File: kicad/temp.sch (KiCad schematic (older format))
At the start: 44 parts, among them U901 ADM2483, U902 AMC1311B, U903 AMC1311B, U904 AMC1311B, U905 AMC1311B

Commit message: changing single row terminal block to double row
I've changed to double row all the connectors, RJ45 and terminal blocks,
I saves spaces and also make it more intuitive related to user
interface..lets go
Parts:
- renumbered C909 to C902, C910 to C904, C907 to C905, C911 to C906, C905 to C907, C912 to C908, C902 to C909, C913 to C910, C904 to C911, C914 to C912, C906 to C913, C915 to C914, C908 to C915, R914 to R903, R915 to R904, R908 to R905, R916 to R906, R905 to R907, R906 to R908, R907 to R909, R917 to R912, R918 to R913, R903 to R914, R904 to R915, R919 to R916, R920 to R917, R909 to R918, R921 to R919, R912 to R920, R913 to R921, U902 to U901, U904 to U902, U901 to U903, U903 to U904

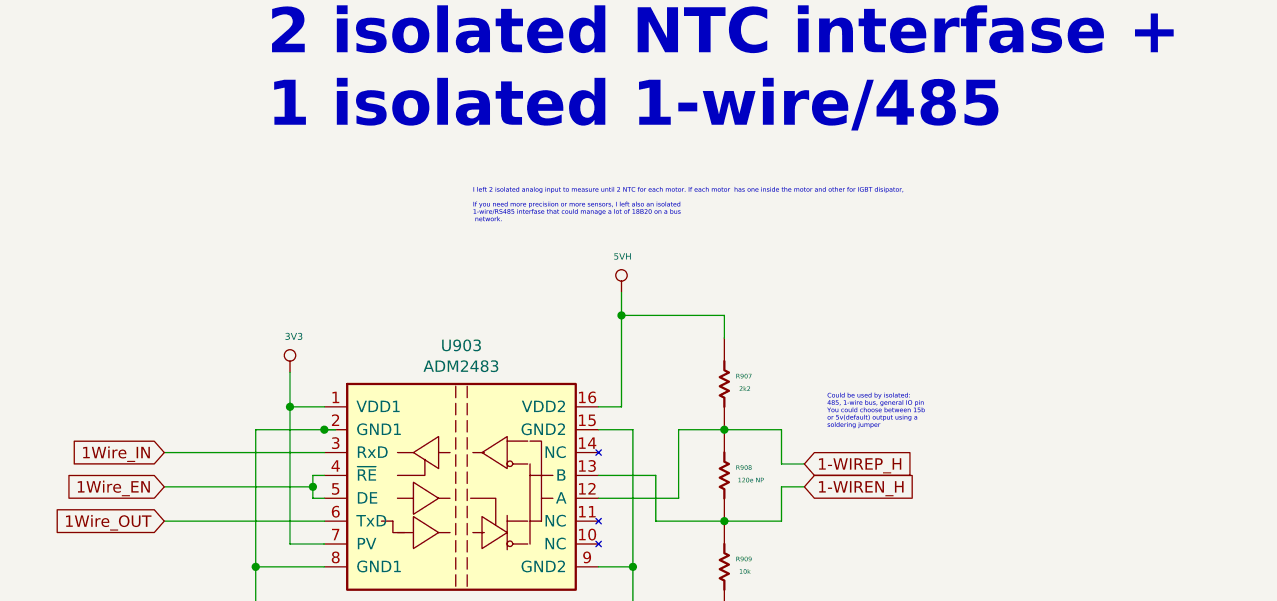
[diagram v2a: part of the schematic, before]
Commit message: placing smmall capacitors and resistors nerar his group
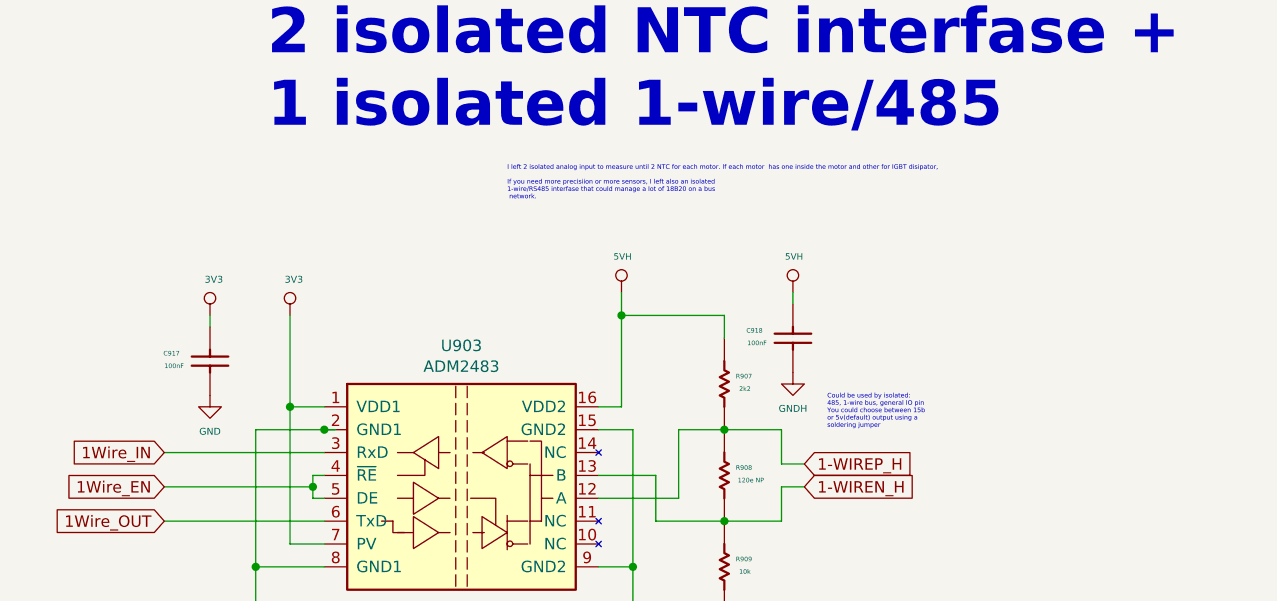
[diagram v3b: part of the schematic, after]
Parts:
- added C917, C918: 100nF, servo:C_0603_1608Metric, symbol servo:Capacitor
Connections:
- net 3V3: now also C917.2 (Capacitor)
- net 5VH: now also C918.2 (Capacitor)
- net GND: now also C917.1
- net GNDH: now also C918.1
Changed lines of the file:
@@
 	9250 3000 9000 3000
-Wire Wire Line
-	8550 2100 9000 2100
 Wire Wire Line
 	9000 2100 9000 2200
@@
 L servo:3V3 #PWR?
 U 1 1 5E0A4BCB
-P 7100 2350
+P 7100 2100
 AR Path="/5DCD812E/5E0A4BCB" Ref="#PWR?"  Part="1"
 AR Path="/5DD4DF4C/5E0A4BCB" Ref="#PWR?"  Part="1"
 AR Path="/5DE49152/5E0A4BCB" Ref="#PWR0905"  Part="1"
-F 0 "#PWR0905" H 7117 2559 20  0001 C CNN
-F 1 "3V3" H 7117 2507 30  0000 C CNN
-F 2 "" H 7100 2350 70  0000 C CNN
-F 3 "" H 7100 2350 70  0000 C CNN
-	1    7100 2350
+F 0 "#PWR0905" H 7117 2309 20  0001 C CNN
+F 1 "3V3" H 7117 2257 30  0000 C CNN
+F 2 "" H 7100 2100 70  0000 C CNN
+F 3 "" H 7100 2100 70  0000 C CNN
+	1    7100 2100
 	1    0    0    -1
 $EndComp
@@
 	8300 4950 8300 5600
 Wire Wire Line
-	7100 2350 7100 2500
+	7100 2100 7100 2500
 Wire Wire Line
 	8550 2000 8550 2100
@@
 Wire Wire Line
 	11500 4650 11250 4650
-Text Notes 7900 1700 0    20   ~ 0
+Text Notes 8050 1600 0    20   ~ 0
 I left 2 isolated analog input to measure until 2 NTC for each motor. If each motor  has one inside the motor and other for IGBT disipator,\n\nIf you need more precisiion or more sensors, I left also an isolated \n1-wire/RS485 interfase that could manage a lot of 18B20 on a bus\n network.\n
 Wire Wire Line
@@
 	1    0    0    -1
 $EndComp
+Wire Wire Line
+	9300 2000 9300 2050
+$Comp
+L servo:Capacitor C?
+U 1 1 5E31D563
+P 9300 2150
+AR Path="/5DEE980E/5E31D563" Ref="C?"  Part="1"
+AR Path="/5E2F3BE3/5E31D563" Ref="C?"  Part="1"
+AR Path="/605BEC04/5E31D563" Ref="C?"  Part="1"
+AR Path="/5DE49152/5E31D563" Ref="C918"  Part="1"
+F 0 "C918" V 9328 1946 20  0000 L BNN
+F 1 "100nF" V 9371 1993 20  0000 C CNN
+F 2 "servo:C_0603_1608Metric" H 9300 2050 60  0001 C CNN
+F 3 "" H 9300 2150 60  0000 C CNN
+	1    9300 2150
+	0    1    1    0
+$EndComp
+$Comp
+L servo:5VH #PWR0189
+U 1 1 5E3339D7
+P 9300 2000
+F 0 "#PWR0189" H 9300 1800 20  0001 C CNN
+F 1 "5VH" H 9305 2157 28  0000 C CNN
+F 2 "" H 9300 2000 50  0001 C CNN
+F 3 "" H 9300 2000 50  0001 C CNN
+	1    9300 2000
+	1    0    0    -1
+$EndComp
+Wire Wire Line
+	8550 2100 9000 2100
+$Comp
+L servo:GNDH #PWR0190
+U 1 1 5E333B21
+P 9300 2350
+F 0 "#PWR0190" H 9300 2100 30  0001 C CNN
+F 1 "GNDH" H 9300 2192 30  0000 C CNN
+F 2 "" H 9300 2350 50  0001 C CNN
+F 3 "" H 9300 2350 50  0001 C CNN
+	1    9300 2350
+	1    0    0    -1
+$EndComp
+Wire Wire Line
+	6750 2100 6750 2150
+$Comp
+L servo:Capacitor C?
+U 1 1 5E33EC9B
+P 6750 2250
+AR Path="/5DEE980E/5E33EC9B" Ref="C?"  Part="1"
+AR Path="/5E2F3BE3/5E33EC9B" Ref="C?"  Part="1"
+AR Path="/605BEC04/5E33EC9B" Ref="C?"  Part="1"
+AR Path="/5DE49152/5E33EC9B" Ref="C917"  Part="1"
+F 0 "C917" V 6778 2046 20  0000 L BNN
+F 1 "100nF" V 6821 2093 20  0000 C CNN
+F 2 "servo:C_0603_1608Metric" H 6750 2150 60  0001 C CNN
+F 3 "" H 6750 2250 60  0000 C CNN
+	1    6750 2250
+	0    1    1    0
+$EndComp
+$Comp
+L servo:3V3 #PWR?
+U 1 1 5E349DDD
+P 6750 2100
+AR Path="/5DCD812E/5E349DDD" Ref="#PWR?"  Part="1"
+AR Path="/5DD4DF4C/5E349DDD" Ref="#PWR?"  Part="1"
+AR Path="/5DE49152/5E349DDD" Ref="#PWR0192"  Part="1"
+F 0 "#PWR0192" H 6767 2309 20  0001 C CNN
+F 1 "3V3" H 6767 2257 30  0000 C CNN
+F 2 "" H 6750 2100 70  0000 C CNN
+F 3 "" H 6750 2100 70  0000 C CNN
+	1    6750 2100
+	1    0    0    -1
+$EndComp
+$Comp
+L servo:GND #PWR_?
+U 1 1 5E3E3460
+P 6750 2450
+AR Path="/5DD4DF4C/5E3E3460" Ref="#PWR_?"  Part="1"
+AR Path="/5DE49152/5E3E3460" Ref="#PWR_0101"  Part="1"
+F 0 "#PWR_0101" H 6755 2301 20  0001 C CNN
+F 1 "GND" H 6750 2292 30  0000 C CNN
+F 2 "" H 6750 2450 70  0000 C CNN
+F 3 "" H 6750 2450 70  0000 C CNN
+	1    6750 2450
+	1    0    0    -1
+$EndComp

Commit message: beginine routing... far far away
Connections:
- net 1-WIREN_H renamed 1-WIRE_N_H
- net 1-WIREP_H renamed 1-WIRE_P_H
- net 1Wire_EN renamed 1WIRE_EN
- net 1Wire_IN renamed 1WIRE_IN
- net 1Wire_OUT renamed 1WIRE_OUT
- net NTCA1_H renamed NTC1_1_H
- net NTCA1_N renamed NTC1_1_N
- net NTCA1_P renamed NTC1_1_P
- net NTCA2_H renamed NTC1_2_H
- net NTCA2_N renamed NTC1_2_N
- net NTCA2_P renamed NTC1_2_P
- net NTCB1_H renamed NTC2_1_H
- net NTCB1_N renamed NTC2_1_N
- net NTCB1_P renamed NTC2_1_P
- net NTCB2_H renamed NTC2_2_H
- net NTCB2_N renamed NTC2_2_N
- net NTCB2_P renamed NTC2_2_P
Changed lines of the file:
@@
 $EndDescr
 Text GLabel 6550 3000 0    50   Input ~ 0
-1Wire_OUT
+1WIRE_OUT
 Text GLabel 6550 2700 0    50   Input ~ 0
-1Wire_IN
+1WIRE_IN
 $Comp
 L servo:ADM2483 U903
@@
 	7250 2700 6550 2700
 Text GLabel 6550 2850 0    50   Input ~ 0
-1Wire_EN
+1WIRE_EN
 Wire Wire Line
 	7250 2800 7200 2800
@@
 Connection ~ 6950 4950
 Text GLabel 5950 4600 0    50   Input ~ 0
-NTCA1_P
+NTC1_1_P
 Text GLabel 5950 5000 0    50   Input ~ 0
-NTCA1_N
+NTC1_1_N
 $Comp
 L servo:AMC1311B U901
@@
 Wire Wire Line
 	6750 4850 7200 4850
-Text GLabel 9400 5050 2    50   Input ~ 0
-NTCA1_H
 $Comp
 L servo:5VH #PWR0906
@@
 Connection ~ 12750 4950
 Text GLabel 13750 4600 2    50   Input ~ 0
-NTCB1_P
+NTC2_1_P
 Text GLabel 13750 5000 2    50   Input ~ 0
-NTCB1_N
+NTC2_1_N
 $Comp
 L servo:AMC1311B U904
@@
 Wire Wire Line
 	12950 4850 12500 4850
-Text GLabel 10300 5050 0    50   Input ~ 0
-NTCB1_H
 $Comp
 L servo:5VH #PWR0914
@@
 	10450 5050 10300 5050
 Text GLabel 9350 2750 2    50   Input ~ 0
-1-WIREP_H
+1-WIRE_P_H
 Text GLabel 9350 2850 2    50   Input ~ 0
-1-WIREN_H
+1-WIRE_N_H
 Wire Wire Line
 	9250 2750 9350 2750
@@
 Connection ~ 6950 6600
 Text GLabel 5950 6250 0    50   Input ~ 0
-NTCA2_P
+NTC1_2_P
 Text GLabel 5950 6650 0    50   Input ~ 0
-NTCA2_N
+NTC1_2_N
 $Comp
 L servo:AMC1311B U902
@@
 Wire Wire Line
 	6750 6500 7200 6500
-Text GLabel 9400 6700 2    50   Input ~ 0
-NTCA2_H
 $Comp
 L servo:5VH #PWR0907
@@
 Connection ~ 12750 6600
 Text GLabel 13750 6250 2    50   Input ~ 0
-NTCB2_P
+NTC2_2_P
 Text GLabel 13750 6650 2    50   Input ~ 0
-NTCB2_N
+NTC2_2_N
 $Comp
 L servo:AMC1311B U905
@@
 Wire Wire Line
 	12950 6500 12500 6500
-Text GLabel 10300 6700 0    50   Input ~ 0
-NTCB2_H
 $Comp
 L servo:5VH #PWR0915
@@
 	1    0    0    -1
 $EndComp
+Text GLabel 9400 5050 2    50   Input ~ 0
+NTC1_1_H
+Text GLabel 9400 6700 2    50   Input ~ 0
+NTC1_2_H
+Text GLabel 10300 6700 0    50   Input ~ 0
+NTC2_2_H
+Text GLabel 10300 5050 0    50   Input ~ 0
+NTC2_1_H
 $EndSCHEMATC

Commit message: change in 5v interface scenario.. remove bridges
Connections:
- net 5VH renamed 5VP
- net GNDH renamed GNDP
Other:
- moved on the sheet: C918

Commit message: serigrafia...
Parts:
- R901, R902, R903, R904, R905, R906, R907, R908, R909, R910, R911, R912, R913, R914, R915, R916, R917, R918, R919, R920, R921, R922, R923: footprint Resistor_SMD:R_0603_1608Metric -> servo:R_0603_1608Metric
- U901, U902, U904, U905: footprint Package_SO:SSO-8_9.6x6.3mm_P1.27mm_Clearance10.5mm -> servo:SSO-8_6.8x5.9mm_P1.27mm_Clearance8mm
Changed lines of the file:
@@
 F 0 "R908" V 8978 2850 20  0000 L BNN
 F 1 "120e NP" V 9021 2916 20  0000 C CNN
-F 2 "Resistor_SMD:R_0603_1608Metric" H 8500 2700 60  0001 C CNN
+F 2 "servo:R_0603_1608Metric" H 8500 2700 60  0001 C CNN
 F 3 "" H 8600 2800 60  0001 C CNN
 	1    9000 2800
@@
 F 0 "R909" V 8978 3250 20  0000 L BNN
 F 1 "10k" V 9021 3290 20  0000 C CNN
-F 2 "Resistor_SMD:R_0603_1608Metric" H 8500 3100 60  0001 C CNN
+F 2 "servo:R_0603_1608Metric" H 8500 3100 60  0001 C CNN
 F 3 "" H 8600 3200 60  0001 C CNN
 	1    9000 3200
@@
 F 0 "R907" V 8978 2450 20  0000 L BNN
 F 1 "2k2" V 9021 2490 20  0000 C CNN
-F 2 "Resistor_SMD:R_0603_1608Metric" H 8500 2300 60  0001 C CNN
+F 2 "servo:R_0603_1608Metric" H 8500 2300 60  0001 C CNN
 F 3 "" H 8600 2400 60  0001 C CNN
 	1    9000 2400
@@
 F 0 "R911" V 9228 5400 20  0000 L BNN
 F 1 "10k" V 9271 5440 20  0000 C CNN
-F 2 "Resistor_SMD:R_0603_1608Metric" H 8750 5250 60  0001 C CNN
+F 2 "servo:R_0603_1608Metric" H 8750 5250 60  0001 C CNN
 F 3 "" H 8850 5350 60  0001 C CNN
 	1    9250 5350
@@
 F 0 "R905" H 8910 5165 20  0000 L BNN
 F 1 "12e" H 8950 5122 20  0000 C CNN
-F 2 "Resistor_SMD:R_0603_1608Metric" H 8450 4950 60  0001 C CNN
+F 2 "servo:R_0603_1608Metric" H 8450 4950 60  0001 C CNN
 F 3 "" H 8550 5050 60  0001 C CNN
 	1    8950 5050
@@
 F 0 "U901" H 7700 5067 50  0000 C CNN
 F 1 "AMC1311B" H 7700 4976 50  0000 C CNN
-F 2 "Package_SO:SSO-8_9.6x6.3mm_P1.27mm_Clearance10.5mm" H 7750 3700 50  0001 C CIN
+F 2 "servo:SSO-8_6.8x5.9mm_P1.27mm_Clearance8mm" H 7750 3700 50  0001 C CIN
 F 3 "../doc/datasheets/amc1311.pdf" H 7650 4200 50  0001 C CNN
 	1    7700 4700
@@
 F 0 "R910" V 9228 4900 20  0000 L BNN
 F 1 "1k(dnp)" V 9271 4940 20  0000 C CNN
-F 2 "Resistor_SMD:R_0603_1608Metric" H 8750 4750 60  0001 C CNN
+F 2 "servo:R_0603_1608Metric" H 8750 4750 60  0001 C CNN
 F 3 "" H 8850 4850 60  0001 C CNN
 	1    9250 4850
@@
 F 0 "R901" H 6421 4485 20  0000 L BNN
 F 1 "2k2" H 6450 4528 20  0000 C CNN
-F 2 "Resistor_SMD:R_0603_1608Metric" H 5950 4500 60  0001 C CNN
+F 2 "servo:R_0603_1608Metric" H 5950 4500 60  0001 C CNN
 F 3 "" H 6050 4600 60  0001 C CNN
 	1    6450 4600
@@
 F 0 "R902" H 6421 4885 20  0000 L BNN
 F 1 "2k2" H 6450 4928 20  0000 C CNN
-F 2 "Resistor_SMD:R_0603_1608Metric" H 5950 4900 60  0001 C CNN
+F 2 "servo:R_0603_1608Metric" H 5950 4900 60  0001 C CNN
 F 3 "" H 6050 5000 60  0001 C CNN
 	1    6450 5000
@@
 F 0 "R915" V 10428 5400 20  0000 L BNN
 F 1 "10k" V 10471 5440 20  0000 C CNN
-F 2 "Resistor_SMD:R_0603_1608Metric" H 9950 5250 60  0001 C CNN
+F 2 "servo:R_0603_1608Metric" H 9950 5250 60  0001 C CNN
 F 3 "" H 10050 5350 60  0001 C CNN
 	1    10450 5350
@@
 F 0 "R918" H 10710 5165 20  0000 L BNN
 F 1 "12e" H 10750 5122 20  0000 C CNN
-F 2 "Resistor_SMD:R_0603_1608Metric" H 10250 4950 60  0001 C CNN
+F 2 "servo:R_0603_1608Metric" H 10250 4950 60  0001 C CNN
 F 3 "" H 10350 5050 60  0001 C CNN
 	1    10750 5050
@@
 F 0 "U904" H 12000 5067 50  0000 C CNN
 F 1 "AMC1311B" H 12000 4976 50  0000 C CNN
-F 2 "Package_SO:SSO-8_9.6x6.3mm_P1.27mm_Clearance10.5mm" H 12050 3700 50  0001 C CIN
+F 2 "servo:SSO-8_6.8x5.9mm_P1.27mm_Clearance8mm" H 12050 3700 50  0001 C CIN
 F 3 "../doc/datasheets/amc1311.pdf" H 11950 4200 50  0001 C CNN
 	1    12000 4700
@@
 F 0 "R914" V 10428 4900 20  0000 L BNN
 F 1 "1k(dnp)" V 10471 4940 20  0000 C CNN
-F 2 "Resistor_SMD:R_0603_1608Metric" H 9950 4750 60  0001 C CNN
+F 2 "servo:R_0603_1608Metric" H 9950 4750 60  0001 C CNN
 F 3 "" H 10050 4850 60  0001 C CNN
 	1    10450 4850
@@
 F 0 "R920" H 13221 4485 20  0000 L BNN
 F 1 "2k2" H 13250 4528 20  0000 C CNN
-F 2 "Resistor_SMD:R_0603_1608Metric" H 12750 4500 60  0001 C CNN
+F 2 "servo:R_0603_1608Metric" H 12750 4500 60  0001 C CNN
 F 3 "" H 12850 4600 60  0001 C CNN
 	1    13250 4600
@@
 F 0 "R921" H 13221 4885 20  0000 L BNN
 F 1 "2k2" H 13250 4928 20  0000 C CNN
-F 2 "Resistor_SMD:R_0603_1608Metric" H 12750 4900 60  0001 C CNN
+F 2 "servo:R_0603_1608Metric" H 12750 4900 60  0001 C CNN
 F 3 "" H 12850 5000 60  0001 C CNN
 	1    13250 5000
@@
 F 0 "R913" V 9228 7050 20  0000 L BNN
 F 1 "10k" V 9271 7090 20  0000 C CNN
-F 2 "Resistor_SMD:R_0603_1608Metric" H 8750 6900 60  0001 C CNN
+F 2 "servo:R_0603_1608Metric" H 8750 6900 60  0001 C CNN
 F 3 "" H 8850 7000 60  0001 C CNN
 	1    9250 7000
@@
 F 0 "R906" H 8910 6815 20  0000 L BNN
 F 1 "12e" H 8950 6772 20  0000 C CNN
-F 2 "Resistor_SMD:R_0603_1608Metric" H 8450 6600 60  0001 C CNN
+F 2 "servo:R_0603_1608Metric" H 8450 6600 60  0001 C CNN
 F 3 "" H 8550 6700 60  0001 C CNN
 	1    8950 6700
@@
 F 0 "U902" H 7700 6717 50  0000 C CNN
 F 1 "AMC1311B" H 7700 6626 50  0000 C CNN
-F 2 "Package_SO:SSO-8_9.6x6.3mm_P1.27mm_Clearance10.5mm" H 7750 5350 50  0001 C CIN
+F 2 "servo:SSO-8_6.8x5.9mm_P1.27mm_Clearance8mm" H 7750 5350 50  0001 C CIN
 F 3 "../doc/datasheets/amc1311.pdf" H 7650 5850 50  0001 C CNN
 	1    7700 6350
@@
 F 0 "R912" V 9228 6550 20  0000 L BNN
 F 1 "1k(dnp)" V 9271 6590 20  0000 C CNN
-F 2 "Resistor_SMD:R_0603_1608Metric" H 8750 6400 60  0001 C CNN
+F 2 "servo:R_0603_1608Metric" H 8750 6400 60  0001 C CNN
 F 3 "" H 8850 6500 60  0001 C CNN
 	1    9250 6500
@@
 F 0 "R903" H 6421 6135 20  0000 L BNN
 F 1 "2k2" H 6450 6178 20  0000 C CNN
-F 2 "Resistor_SMD:R_0603_1608Metric" H 5950 6150 60  0001 C CNN
+F 2 "servo:R_0603_1608Metric" H 5950 6150 60  0001 C CNN
 F 3 "" H 6050 6250 60  0001 C CNN
 	1    6450 6250
@@
 F 0 "R904" H 6421 6535 20  0000 L BNN
 F 1 "2k2" H 6450 6578 20  0000 C CNN
-F 2 "Resistor_SMD:R_0603_1608Metric" H 5950 6550 60  0001 C CNN
+F 2 "servo:R_0603_1608Metric" H 5950 6550 60  0001 C CNN
 F 3 "" H 6050 6650 60  0001 C CNN
 	1    6450 6650
@@
 F 0 "R917" V 10428 7050 20  0000 L BNN
 F 1 "10k" V 10471 7090 20  0000 C CNN
-F 2 "Resistor_SMD:R_0603_1608Metric" H 9950 6900 60  0001 C CNN
+F 2 "servo:R_0603_1608Metric" H 9950 6900 60  0001 C CNN
 F 3 "" H 10050 7000 60  0001 C CNN
 	1    10450 7000
@@
 F 0 "R919" H 10710 6815 20  0000 L BNN
 F 1 "12e" H 10750 6772 20  0000 C CNN
-F 2 "Resistor_SMD:R_0603_1608Metric" H 10250 6600 60  0001 C CNN
+F 2 "servo:R_0603_1608Metric" H 10250 6600 60  0001 C CNN
 F 3 "" H 10350 6700 60  0001 C CNN
 	1    10750 6700
@@
 F 0 "U905" H 12000 6717 50  0000 C CNN
 F 1 "AMC1311B" H 12000 6626 50  0000 C CNN
-F 2 "Package_SO:SSO-8_9.6x6.3mm_P1.27mm_Clearance10.5mm" H 12050 5350 50  0001 C CIN
+F 2 "servo:SSO-8_6.8x5.9mm_P1.27mm_Clearance8mm" H 12050 5350 50  0001 C CIN
 F 3 "../doc/datasheets/amc1311.pdf" H 11950 5850 50  0001 C CNN
 	1    12000 6350
@@
 F 0 "R916" V 10428 6550 20  0000 L BNN
 F 1 "1k(dnp)" V 10471 6590 20  0000 C CNN
-F 2 "Resistor_SMD:R_0603_1608Metric" H 9950 6400 60  0001 C CNN
+F 2 "servo:R_0603_1608Metric" H 9950 6400 60  0001 C CNN
 F 3 "" H 10050 6500 60  0001 C CNN
 	1    10450 6500
@@
 F 0 "R922" H 13221 6135 20  0000 L BNN
 F 1 "2k2" H 13250 6178 20  0000 C CNN
-F 2 "Resistor_SMD:R_0603_1608Metric" H 12750 6150 60  0001 C CNN
+F 2 "servo:R_0603_1608Metric" H 12750 6150 60  0001 C CNN
 F 3 "" H 12850 6250 60  0001 C CNN
 	1    13250 6250
@@
 F 0 "R923" H 13221 6535 20  0000 L BNN
 F 1 "2k2" H 13250 6578 20  0000 C CNN
-F 2 "Resistor_SMD:R_0603_1608Metric" H 12750 6550 60  0001 C CNN
+F 2 "servo:R_0603_1608Metric" H 12750 6550 60  0001 C CNN
 F 3 "" H 12850 6650 60  0001 C CNN
 	1    13250 6650

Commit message: serigraphi, improve of nets. change of soic 8 footprint
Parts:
- U901, U902, U904, U905: footprint servo:SSO-8_6.8x5.9mm_P1.27mm_Clearance8mm -> servo:SSO-8_7.6x5.9mm_P1.27mm_Clearance9.1mm
- U903: footprint Package_SO:SOIC-16W_7.5x10.3mm_P1.27mm -> servo:SOIC-16W_7.5x10.3mm_P1.27mm
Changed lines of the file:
@@
 F 0 "U903" H 7850 3467 50  0000 C CNN
 F 1 "ADM2483" H 7850 3376 50  0000 C CNN
-F 2 "Package_SO:SOIC-16W_7.5x10.3mm_P1.27mm" H 7850 2150 50  0001 C CNN
+F 2 "servo:SOIC-16W_7.5x10.3mm_P1.27mm" H 7850 2150 50  0001 C CNN
 F 3 "../doc/datasheets/adm2483.pdf" H 7100 2750 50  0001 C CNN
 	1    7850 2850
@@
 F 0 "U901" H 7700 5067 50  0000 C CNN
 F 1 "AMC1311B" H 7700 4976 50  0000 C CNN
-F 2 "servo:SSO-8_6.8x5.9mm_P1.27mm_Clearance8mm" H 7750 3700 50  0001 C CIN
+F 2 "servo:SSO-8_7.6x5.9mm_P1.27mm_Clearance9.1mm" H 7750 3700 50  0001 C CIN
 F 3 "../doc/datasheets/amc1311.pdf" H 7650 4200 50  0001 C CNN
 	1    7700 4700
@@
 F 0 "U904" H 12000 5067 50  0000 C CNN
 F 1 "AMC1311B" H 12000 4976 50  0000 C CNN
-F 2 "servo:SSO-8_6.8x5.9mm_P1.27mm_Clearance8mm" H 12050 3700 50  0001 C CIN
+F 2 "servo:SSO-8_7.6x5.9mm_P1.27mm_Clearance9.1mm" H 12050 3700 50  0001 C CIN
 F 3 "../doc/datasheets/amc1311.pdf" H 11950 4200 50  0001 C CNN
 	1    12000 4700
@@
 F 0 "U902" H 7700 6717 50  0000 C CNN
 F 1 "AMC1311B" H 7700 6626 50  0000 C CNN
-F 2 "servo:SSO-8_6.8x5.9mm_P1.27mm_Clearance8mm" H 7750 5350 50  0001 C CIN
+F 2 "servo:SSO-8_7.6x5.9mm_P1.27mm_Clearance9.1mm" H 7750 5350 50  0001 C CIN
 F 3 "../doc/datasheets/amc1311.pdf" H 7650 5850 50  0001 C CNN
 	1    7700 6350
@@
 F 0 "U905" H 12000 6717 50  0000 C CNN
 F 1 "AMC1311B" H 12000 6626 50  0000 C CNN
-F 2 "servo:SSO-8_6.8x5.9mm_P1.27mm_Clearance8mm" H 12050 5350 50  0001 C CIN
+F 2 "servo:SSO-8_7.6x5.9mm_P1.27mm_Clearance9.1mm" H 12050 5350 50  0001 C CIN
 F 3 "../doc/datasheets/amc1311.pdf" H 11950 5850 50  0001 C CNN
 	1    12000 6350
